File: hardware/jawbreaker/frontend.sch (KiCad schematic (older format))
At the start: 115 parts, among them P2 SERIAL, P4 ANTENNA, P5 CLK, P6 SWITCH_CTRL, P7 VCC, Q1 MOSFET_P, Q2 MOSFET_P, T1 MIX_IN_BALUN, T2 MIX_OUT_BALUN, U1 SKY13350, U10 SKY13350, U11 SKY13350, U12 SKY13317, U13 MGA-81563, U14 SKY13317, U15 GSG-74HC04, U16 GSG-74HC08, U2 SKY13350, U25 MGA-81563, U3 RX_LOWPASS_FILTER, U4 RFFC5072, U5 SKY13350, U6 SKY13350, U7 SKY13350, U8 RX_HIGHPASS_FILTER, U9 SKY13317

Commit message: MIX_CLK instead of headers
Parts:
- removed P5: CLK, symbol CONN_2
- removed P7: VCC, symbol CONN_7X2
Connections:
- net labels added: MIX_CLK
- net labels removed: CLK
- wire segments 387 -> 368
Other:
- note added: "Expected MIX_CLK is 1.8 to 3.3 V\npeak-to-peak at 25 to 52 MHz. It is\ndivided down to 0.5 to 1.5 V (REF_IN)."
- note removed: "Expected clock input is 1.8 to 3.3 V\npeak-to-peak at 25 to 52 MHz. It is\ndivided down to 0.5 to 1.5 V (REF_IN)."
- moved on the sheet: C67, C70
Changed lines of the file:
@@
-EESchema Schematic File Version 2  date Sun Sep  2 15:42:59 2012
+EESchema Schematic File Version 2  date Sun Sep  2 15:54:35 2012
 LIBS:power
 LIBS:device
@@
 Comment4 ""
 $EndDescr
+Text GLabel 9050 9100 1    40   Input ~ 0
+MIX_CLK
 $Comp
 L VAA #PWR46
@@
 Wire Wire Line
 	3350 4400 3250 4400
-Wire Wire Line
-	8100 9400 8100 9300
-Connection ~ 9850 9950
-Wire Wire Line
-	9850 9350 9850 10050
-Wire Wire Line
-	9850 10050 9750 10050
-Connection ~ 9850 9750
-Wire Wire Line
-	9850 9850 9750 9850
-Connection ~ 9850 9550
-Wire Wire Line
-	9850 9650 9750 9650
-Wire Wire Line
-	9850 9450 9750 9450
-Connection ~ 8850 9650
-Wire Wire Line
-	8850 9550 8950 9550
-Connection ~ 8850 9850
-Wire Wire Line
-	8850 9750 8950 9750
-Connection ~ 8850 10050
-Wire Wire Line
-	8850 9950 8950 9950
 Connection ~ 1850 2700
 Wire Wire Line
@@
 Wire Wire Line
 	15700 9700 15700 9600
-Connection ~ 8350 9700
+Connection ~ 9050 9700
 Wire Wire Line
-	8600 9700 8350 9700
+	9300 9700 9050 9700
 Wire Wire Line
-	8350 9600 8350 9800
+	9050 9600 9050 9800
 Wire Wire Line
 	6700 10050 6800 10050
@@
 	5800 10050 5800 10150
 Wire Wire Line
-	8350 10300 8350 10200
+	9050 10300 9050 10200
 Wire Wire Line
-	8350 9200 8350 9100
+	9050 9200 9050 9100
 Wire Wire Line
 	4350 5950 4350 5850
@@
 Connection ~ 10350 2400
 Wire Wire Line
-	8950 10050 8850 10050
-Wire Wire Line
-	8850 9850 8950 9850
-Connection ~ 8850 9950
-Wire Wire Line
-	8850 9650 8950 9650
-Connection ~ 8850 9750
-Wire Wire Line
-	8850 10150 8850 9450
-Wire Wire Line
-	8850 9450 8950 9450
-Connection ~ 8850 9550
-Wire Wire Line
-	9850 9550 9750 9550
-Connection ~ 9850 9450
-Wire Wire Line
-	9850 9750 9750 9750
-Connection ~ 9850 9650
-Wire Wire Line
-	9750 9950 9850 9950
-Connection ~ 9850 9850
-Wire Wire Line
-	8350 9100 8000 9100
-Wire Wire Line
-	8100 9300 8000 9300
-Wire Wire Line
 	4150 3850 4150 3750
 Wire Wire Line
@@
 $EndComp
 $Comp
-L GND #PWR76
+L GND #PWR74
 U 1 1 502E798B
 P 13700 9500
-F 0 "#PWR76" H 13700 9500 30  0001 C CNN
+F 0 "#PWR74" H 13700 9500 30  0001 C CNN
 F 1 "GND" H 13700 9430 30  0001 C CNN
 	1    13700 9500
@@
 $EndComp
 $Comp
-L GND #PWR75
+L GND #PWR73
 U 1 1 502E798A
 P 13150 9400
-F 0 "#PWR75" H 13150 9400 30  0001 C CNN
+F 0 "#PWR73" H 13150 9400 30  0001 C CNN
 F 1 "GND" H 13150 9330 30  0001 C CNN
 	1    13150 9400
@@
 $EndComp
 $Comp
-L GND #PWR80
+L GND #PWR78
 U 1 1 502E780F
 P 5000 9900
-F 0 "#PWR80" H 5000 9900 30  0001 C CNN
+F 0 "#PWR78" H 5000 9900 30  0001 C CNN
 F 1 "GND" H 5000 9830 30  0001 C CNN
 	1    5000 9900
@@
 MIX_BYPASS
 $Comp
-L GND #PWR88
+L GND #PWR85
 U 1 1 502E772E
 P 3800 10350
-F 0 "#PWR88" H 3800 10350 30  0001 C CNN
+F 0 "#PWR85" H 3800 10350 30  0001 C CNN
 F 1 "GND" H 3800 10280 30  0001 C CNN
 	1    3800 10350
@@
 $EndComp
 $Comp
-L GND #PWR82
+L GND #PWR80
 U 1 1 502E772A
 P 3100 10000
-F 0 "#PWR82" H 3100 10000 30  0001 C CNN
+F 0 "#PWR80" H 3100 10000 30  0001 C CNN
 F 1 "GND" H 3100 9930 30  0001 C CNN
 	1    3100 10000
@@
 	1    0    0    -1
 $EndComp
-$Comp
-L CONN_2 P5
-U 1 1 4FB3CC51
-P 7650 9200
-F 0 "P5" V 7600 9200 40  0000 C CNN
-F 1 "CLK" V 7700 9200 40  0000 C CNN
-F 4 "DNP" H 7650 9200 60  0001 C CNN "Note"
-	1    7650 9200
-	-1   0    0    1
-$EndComp
-$Comp
-L CONN_7X2 P7
-U 1 1 501F4DC6
-P 9350 9750
-F 0 "P7" H 9350 10150 60  0000 C CNN
-F 1 "VCC" V 9350 9750 60  0000 C CNN
-F 4 "DNP" H 9350 9750 60  0001 C CNN "Note"
-	1    9350 9750
-	1    0    0    -1
-$EndComp
 Text Label 1950 6050 3    40   ~ 0
 !MIX_BYPASS
@@
 $EndComp
 $Comp
-L GND #PWR87
+L GND #PWR84
 U 1 1 4FC68E81
 P 1500 10350
-F 0 "#PWR87" H 1500 10350 30  0001 C CNN
+F 0 "#PWR84" H 1500 10350 30  0001 C CNN
 F 1 "GND" H 1500 10280 30  0001 C CNN
 	1    1500 10350
@@
 	1    0    0    -1
 $EndComp
-Text Notes 7050 9600 0    40   ~ 0
-Expected clock input is 1.8 to 3.3 V\npeak-to-peak at 25 to 52 MHz. It is\ndivided down to 0.5 to 1.5 V (REF_IN).
+Text Notes 7750 9600 0    40   ~ 0
+Expected MIX_CLK is 1.8 to 3.3 V\npeak-to-peak at 25 to 52 MHz. It is\ndivided down to 0.5 to 1.5 V (REF_IN).
 $Comp
 L C C70
 U 1 1 4FB3CC76
-P 8350 10000
-F 0 "C70" H 8400 10100 50  0000 L CNN
-F 1 "47pF" H 8400 9900 50  0000 L CNN
-F 4 "Murata" H 8350 9400 60  0001 C CNN "Manufacturer"
-F 5 "GRM1555C1H470JZ01D" H 8350 9400 60  0001 C CNN "Part Number"
-F 6 "CAP CER 47PF 50V 5% NP0 0402" H 8350 9400 60  0001 C CNN "Description"
-	1    8350 10000
+P 9050 10000
+F 0 "C70" H 9100 10100 50  0000 L CNN
+F 1 "47pF" H 9100 9900 50  0000 L CNN
+F 4 "Murata" H 9050 9400 60  0001 C CNN "Manufacturer"
+F 5 "GRM1555C1H470JZ01D" H 9050 9400 60  0001 C CNN "Part Number"
+F 6 "CAP CER 47PF 50V 5% NP0 0402" H 9050 9400 60  0001 C CNN "Description"
+	1    9050 10000
 	1    0    0    -1
 $EndComp
@@
 $EndComp
 $Comp
-L GND #PWR78
+L GND #PWR76
 U 1 1 4FB3F838
 P 15700 9700
-F 0 "#PWR78" H 15700 9700 30  0001 C CNN
+F 0 "#PWR76" H 15700 9700 30  0001 C CNN
 F 1 "GND" H 15700 9630 30  0001 C CNN
 	1    15700 9700
 	1    0    0    -1
 $EndComp
-Text Label 8150 9100 2    40   ~ 0
-CLK
-Text Label 8600 9700 2    40   ~ 0
+Text Label 9300 9700 2    40   ~ 0
 REF_IN
 $Comp
-L GND #PWR86
+L GND #PWR83
 U 1 1 4FB3CC7B
-P 8350 10300
-F 0 "#PWR86" H 8350 10300 30  0001 C CNN
-F 1 "GND" H 8350 10230 30  0001 C CNN
-	1    8350 10300
-	1    0    0    -1
-$EndComp
-$Comp
-L GND #PWR74
-U 1 1 4FB3CC5E
-P 8100 9400
-F 0 "#PWR74" H 8100 9400 30  0001 C CNN
-F 1 "GND" H 8100 9330 30  0001 C CNN
-	1    8100 9400
+P 9050 10300
+F 0 "#PWR83" H 9050 10300 30  0001 C CNN
+F 1 "GND" H 9050 10230 30  0001 C CNN
+	1    9050 10300
 	1    0    0    -1
 $EndComp
 Text Label 5850 2150 3    40   ~ 0
 REF_IN
-$Comp
-L VCC #PWR73
-U 1 1 4FB3CBB2
-P 9850 9350
-F 0 "#PWR73" H 9850 9450 30  0001 C CNN
-F 1 "VCC" H 9850 9450 30  0000 C CNN
-	1    9850 9350
-	1    0    0    -1
-$EndComp
-$Comp
-L GND #PWR85
-U 1 1 4FB3CBAC
-P 8850 10150
-F 0 "#PWR85" H 8850 10150 30  0001 C CNN
-F 1 "GND" H 8850 10080 30  0001 C CNN
-	1    8850 10150
-	1    0    0    -1
-$EndComp
 Text Notes 6700 9200 2    40   ~ 0
 install jumpers for switch\ncontrol via the RFFC5071
@@
 GPO1
 $Comp
-L GND #PWR83
+L GND #PWR81
 U 1 1 4FB3CA7B
 P 5800 10150
-F 0 "#PWR83" H 5800 10150 30  0001 C CNN
+F 0 "#PWR81" H 5800 10150 30  0001 C CNN
 F 1 "GND" H 5800 10080 30  0001 C CNN
 	1    5800 10150
@@
 $EndComp
 $Comp
-L GND #PWR84
+L GND #PWR82
 U 1 1 4FB3CA70
 P 6800 10150
-F 0 "#PWR84" H 6800 10150 30  0001 C CNN
+F 0 "#PWR82" H 6800 10150 30  0001 C CNN
 F 1 "GND" H 6800 10080 30  0001 C CNN
 	1    6800 10150
@@
 $EndComp
 $Comp
-L GND #PWR79
+L GND #PWR77
 U 1 1 4FB2FD23
 P 2450 9900
-F 0 "#PWR79" H 2450 9900 30  0001 C CNN
+F 0 "#PWR77" H 2450 9900 30  0001 C CNN
 F 1 "GND" H 2450 9830 30  0001 C CNN
 	1    2450 9900
@@
 $EndComp
 $Comp
-L GND #PWR81
+L GND #PWR79
 U 1 1 4FB2FD02
 P 800 10000
-F 0 "#PWR81" H 800 10000 30  0001 C CNN
+F 0 "#PWR79" H 800 10000 30  0001 C CNN
 F 1 "GND" H 800 9930 30  0001 C CNN
 	1    800  10000
@@
 L C C67
 U 1 1 4FAECD45
-P 8350 9400
-F 0 "C67" H 8400 9500 50  0000 L CNN
-F 1 "47pF" H 8400 9300 50  0000 L CNN
-F 4 "Murata" H 8350 9400 60  0001 C CNN "Manufacturer"
-F 5 "GRM1555C1H470JZ01D" H 8350 9400 60  0001 C CNN "Part Number"
-F 6 "CAP CER 47PF 50V 5% NP0 0402" H 8350 9400 60  0001 C CNN "Description"
-	1    8350 9400
+P 9050 9400
+F 0 "C67" H 9100 9500 50  0000 L CNN
+F 1 "47pF" H 9100 9300 50  0000 L CNN
+F 4 "Murata" H 9050 9400 60  0001 C CNN "Manufacturer"
+F 5 "GRM1555C1H470JZ01D" H 9050 9400 60  0001 C CNN "Part Number"
+F 6 "CAP CER 47PF 50V 5% NP0 0402" H 9050 9400 60  0001 C CNN "Description"
+	1    9050 9400
 	1    0    0    -1
 $EndComp
@@
 $EndComp
 $Comp
-L GND #PWR77
+L GND #PWR75
 U 1 1 4FAA165E
 P 16400 9600
-F 0 "#PWR77" H 16400 9600 30  0001 C CNN
+F 0 "#PWR75" H 16400 9600 30  0001 C CNN
 F 1 "GND" H 16400 9530 30  0001 C CNN
 	1    16400 9600

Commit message: mixer control traces instead of headers
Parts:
- removed P2: SERIAL, symbol CONN_5X2
- removed P6: SWITCH_CTRL, symbol CONN_7X2
- added P?: GPO4, symbol CONN_1
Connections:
- net labels added: SSP1_MOSI, SSP1_SCLK
- net labels removed: GPO1, GPO2, GPO3, GPO4, GPO5, GPO6, SCLK, SDATA
- wire segments 368 -> 401
- no-connect marks 5 -> 4
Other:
- note removed: "install jumpers for switch\ncontrol via the RFFC5071"
- moved on the sheet: C41, C42, C68, C69, L2, L3, U15, U16

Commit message: PCB antenna
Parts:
- added C?: 10nF, symbol C
- added J?: GSG-900MHZ-F-ANTENNA, symbol GSG-900MHZ-F-ANTENNA
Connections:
- net GND: now also J?.2 (GND)
- net at D1.2 (K), P4.1 (RF): now also C?.2; no longer C64.2
- net at C64.1, U14.1 (RFC): now also C?.1
- new net: C64.2, J?.1 (RF)
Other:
- moved on the sheet: C1, C10, C11, C12, C13, C14, C15, C16, C160, C161, C162, C163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

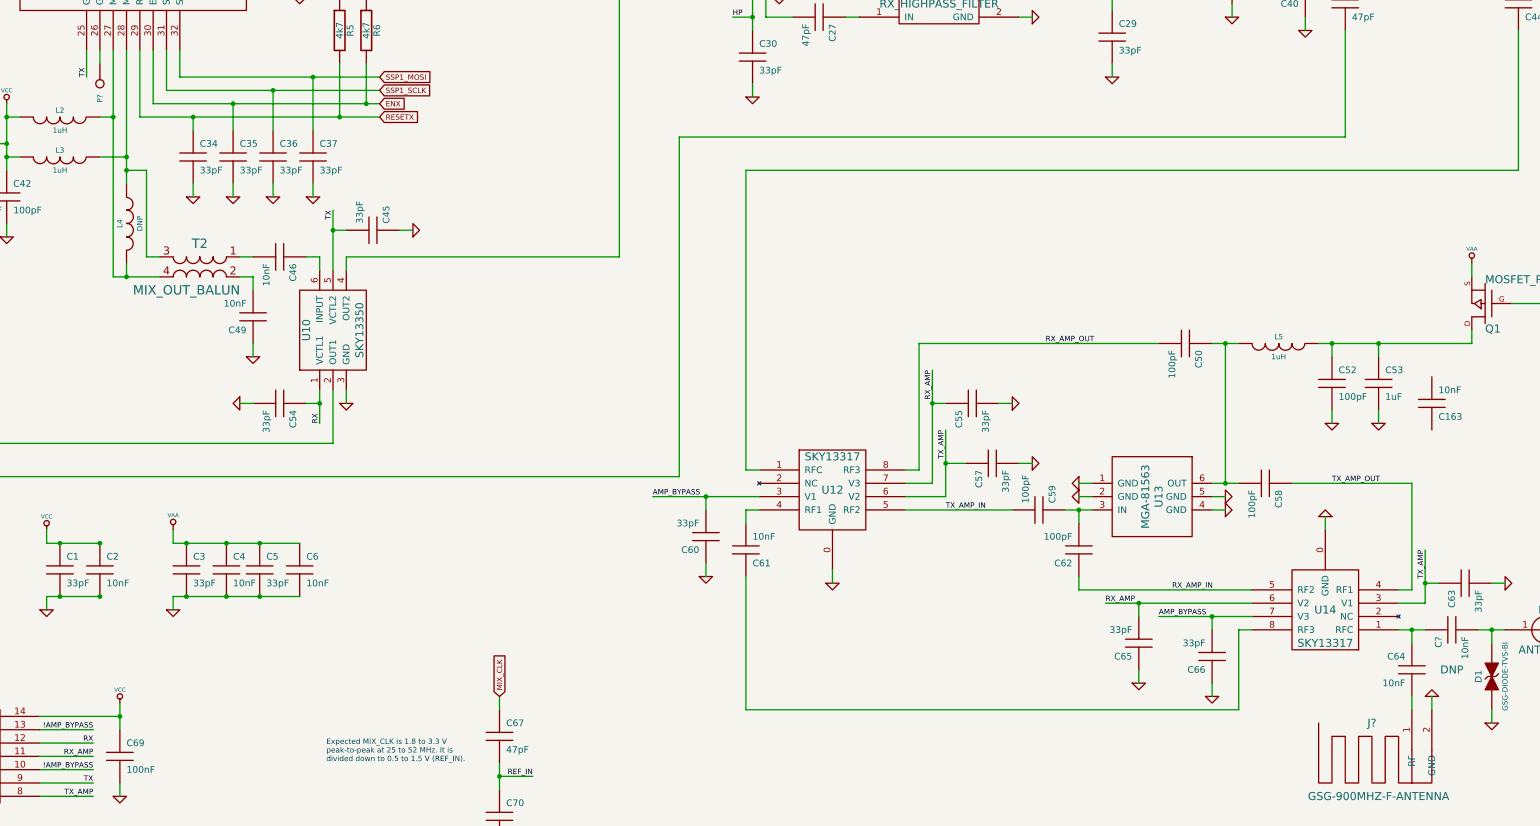
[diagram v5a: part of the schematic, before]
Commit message: reduced expansion headers to save space
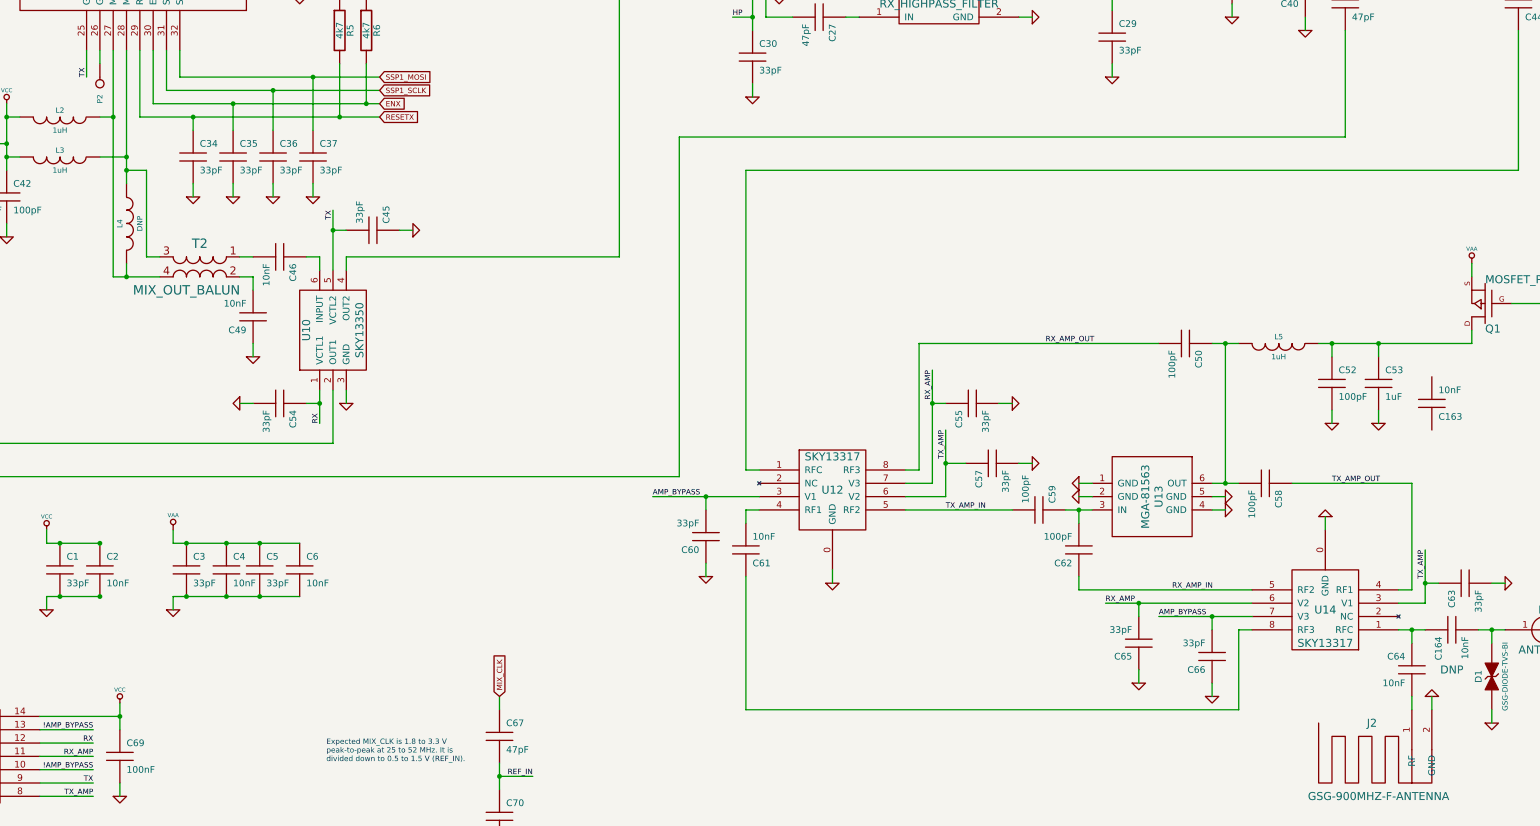
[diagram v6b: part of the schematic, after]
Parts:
- gave numbers to parts that had none: 3

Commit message: back to two amps
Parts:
- removed P2: GPO4, symbol CONN_1
- added R83: 0, symbol R
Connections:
- net AMP_BYPASS: now also C57.1, C65.2, U12.6 (V2), U14.6 (V2); no longer C60.2, C66.2, U12.3 (V1), U14.7 (V3)
- net GND: now also C162.1, C163.1, U25.1 (GND), U25.2 (GND), U25.4 (GND), U25.5 (GND)
- net RX_AMP: now also C63.1, U14.3 (V1); no longer C65.2, U14.6 (V2)
- net RX_AMP_IN: now also C58.1, U14.4 (RF1); no longer C62.1, U14.5 (RF2)
- net TX_AMP: now also C60.2, C66.2, U12.3 (V1), U14.7 (V3); no longer C57.1, C63.1, U12.6 (V2), U14.3 (V1)
- net TX_AMP_IN: now also C59.1, U12.4 (RF1); no longer C59.2, U12.5 (RF2)
- net TX_AMP_OUT: now also C62.1, U14.8 (RF3); no longer C58.1, U14.4 (RF1)
- net VAA: now also C161.1, C53.1, Q2.S, R24.2
- net !RX_AMP_PWR: now reaches U4.26 (GPO4/LD/DO)
- net !RX_AMP_PWR: now also Q1.G, R29.2, R83.1, R83.2
- net at C61.2: now also U12.5 (RF2); no longer U12.4 (RF1)
- net at C61.1: now also U14.5 (RF2); no longer U14.8 (RF3)
- net at C52.1, L5.1, Q1.D: now also C163.2; no longer C53.1
- net at C50.1, L5.2, U13.6 (OUT): no longer C58.2
- net at C162.2: now also C160.1, L12.1, Q2.D
- net !TX_AMP_PWR: now reaches Q2.G
- net !TX_AMP_PWR: now also R24.1, U4.9 (MODE/GPO6)
- net at L12.2: now also C62.2, U25.6 (OUT)
- net at U25.3 (IN): now also C59.2
- removed net !AMP_PWR: Q1.G, R29.2, U4.9 (MODE/GPO6)
- new net: C58.2, U13.3 (IN)
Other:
- moved on the sheet: C160, C161, C162, C163, C164, C23, C50, C52, C53, C55, C57, C59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
